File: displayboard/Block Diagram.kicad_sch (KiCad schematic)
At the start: 0 parts

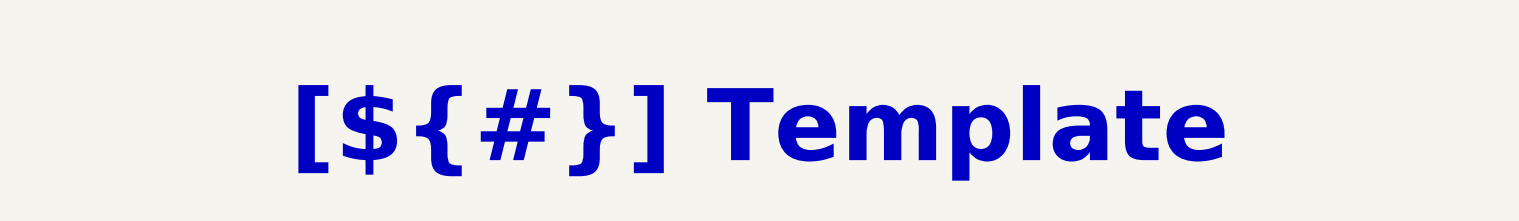
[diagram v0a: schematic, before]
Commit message: Remove old production files, add cutout for the programming cable, add connector for mainboard cable
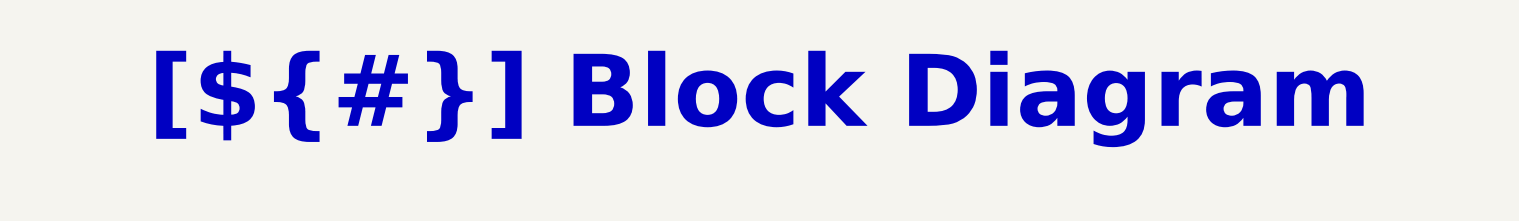
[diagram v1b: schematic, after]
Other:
- title: Template -> Block Diagram
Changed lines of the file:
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@@
 	(paper "A3")
 	(title_block
-		(title "Template")
+		(title "Block Diagram")
 		(date "2025-12-19")
 		(rev "1")
@@
 	(text_box "[${#}] ${TITLE}"
 		(exclude_from_sim no)
-		(at 144.78 20.32 0)
-		(size 130.81 12.7)
+		(at 12.7 12.7 0)
+		(size 394.97 20.32)
 		(margins 5.9999 5.9999 5.9999 5.9999)
 		(stroke
